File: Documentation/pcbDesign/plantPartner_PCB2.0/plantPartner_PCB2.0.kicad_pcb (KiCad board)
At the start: 2 copper layers, 70 x 65.1 mm, 76 parts, among them IC1 MPM3610, J1 Conn_01x04, J10 Screw_Terminal_01x02, J11 Conn_01x02, J12 Conn_01x03, J13 Conn_01x03, J14 Conn_01x03, J15 Conn_01x03, J16 Conn_01x01, J17 Conn_01x03, J18 Conn_01x03, J19 Conn_01x04, J2 Conn_01x04, J20 Conn_01x04, J21 Conn_01x05, J22 Conn_01x04, J23 Conn_01x01, J25 Conn_01x01, J26 Conn_01x01, J27 Conn_01x01, J28 Conn_01x01, J29 Conn_01x02, J3 Conn_01x04, J30 Screw_Terminal_01x02, J4 Screw_Terminal_01x04, J5 Conn_01x02, J6 Barrel_Jack, J7 Screw_Terminal_01x02, J8 Conn_01x01, J9 Screw_Terminal_01x02, Q1 AO3400A, Q2 AO3400A, Q4 AO3400A, U2 MAX485, U3 ESP32-DEVKIT-V1

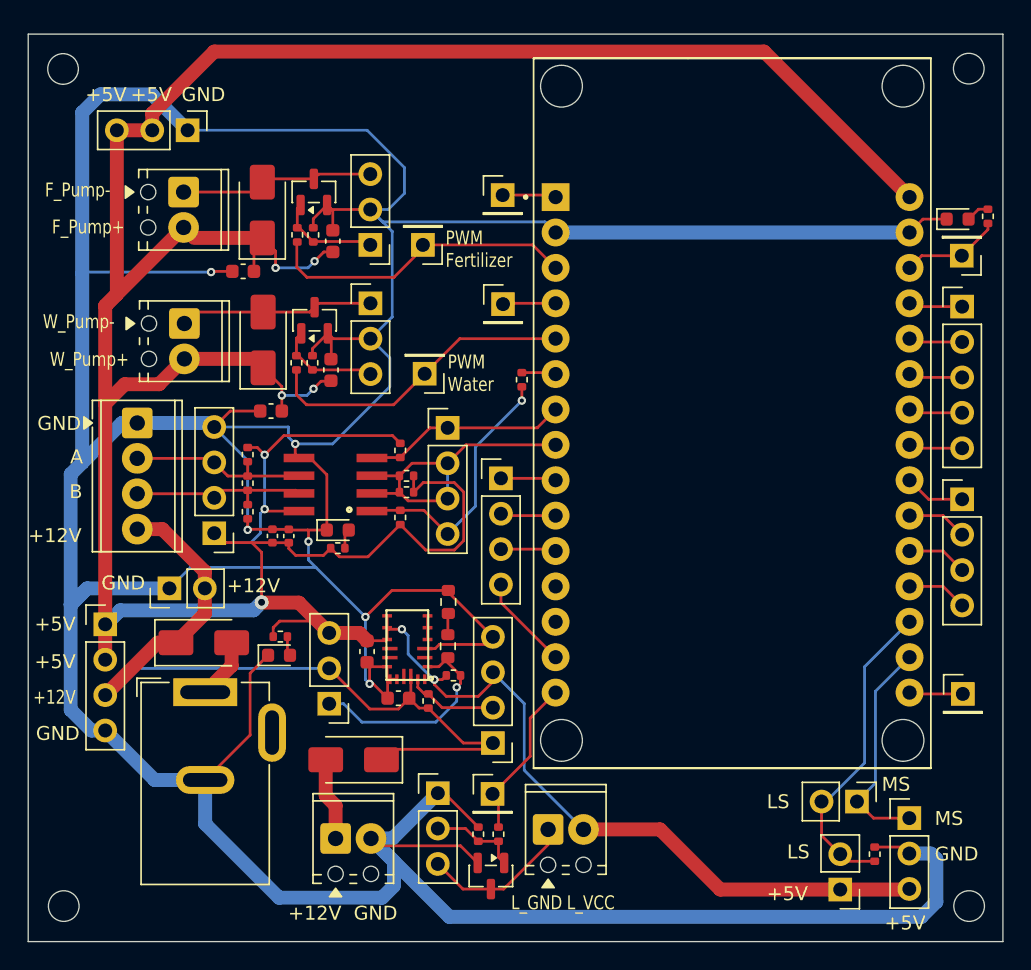
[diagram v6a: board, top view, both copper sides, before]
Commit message: I made an oopsie with PCBv2 order so I had to fix that and in the meantime I found a cheaper solution that kept the same logic of the circuits. It saved us 0 yippee
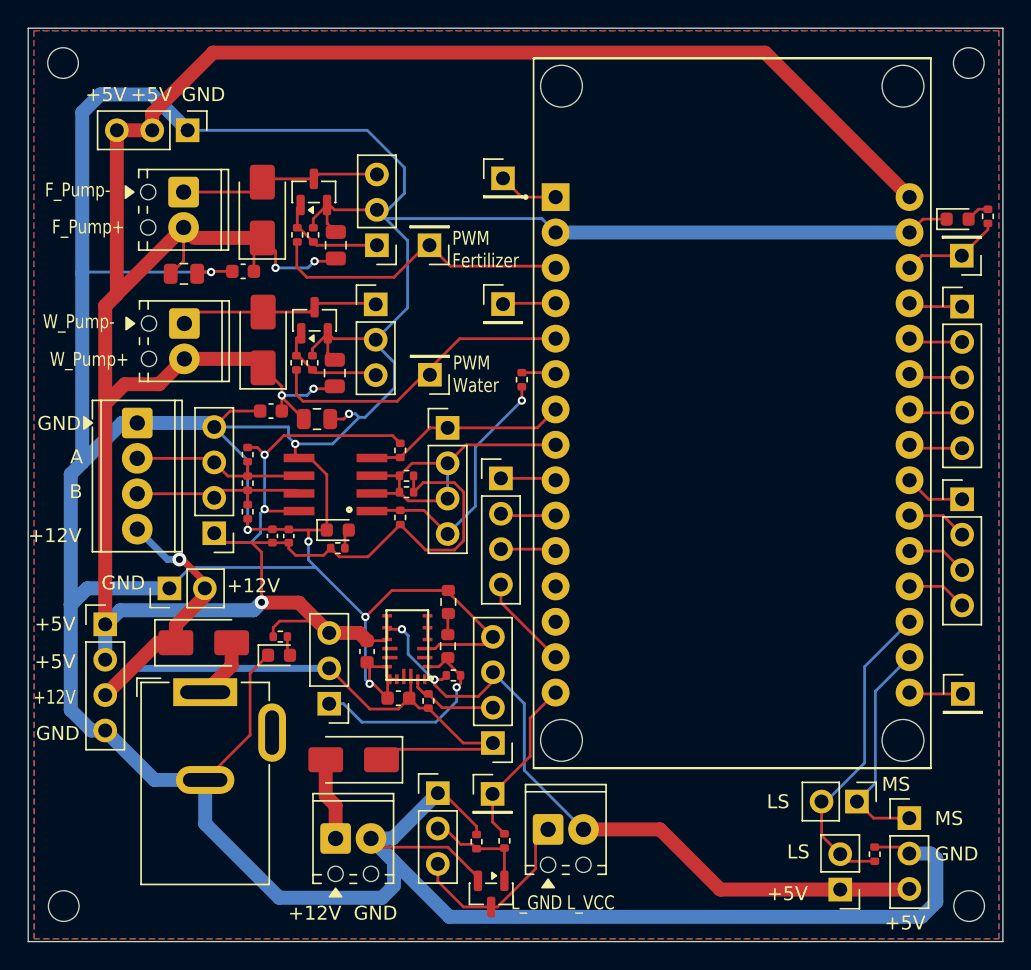
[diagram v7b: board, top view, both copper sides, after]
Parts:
- added C10: 47uF, Capacitor_SMD:C_0805_2012Metric, F.Cu at (71.5, 41.5)
- added C9: 47uF, Capacitor_SMD:C_0805_2012Metric, F.Cu at (81.0, 52.0)
- C5, C6: value 220uF -> 47uF; footprint Capacitor_SMD:C_0603_1608Metric -> Capacitor_SMD:C_0805_2012Metric
- moved Q4 1.28 mm to (93.5, 86.0)
- moved J28 1.20 mm to (94.4, 34.7)
- moved R25 0.64 mm to (94.5, 82.2)
- moved R27 0.55 mm to (92.5, 82.3)
- moved J13 0.48 mm to (85.3, 39.5)
- moved J27 0.48 mm to (89.1, 39.5)
- moved REF** 0.43 mm to (62.8, 26.4)
- moved REF** 0.40 mm to (127.8, 26.4)
- moved J12 0.38 mm to (85.3, 43.7)
- moved J26 0.38 mm to (89.2, 48.8)
- moved C5 0.36 mm to (82.4, 39.5)
- moved C6 0.36 mm to (82.3, 48.6)
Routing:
- net GND: track 381.5 -> 389.1 mm, vias 6 -> 7
- net +5V: track 286.7 -> 294.2 mm
- net /L_Drain: track 11.1 -> 13.4 mm
- net /LAMP_PIN: track 11.7 -> 13.0 mm
- net /L_Gate: track 6.45 -> 7.75 mm
- net /F_Gate: track 7.51 -> 8.37 mm
- net +12V: track 60.3 -> 59.9 mm, vias 0 -> 1
- added copper zone on B.Cu, net GND
- added copper zone on F.Cu, net GND
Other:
- board size 70 x 65.1 mm -> 70 x 65.6 mm

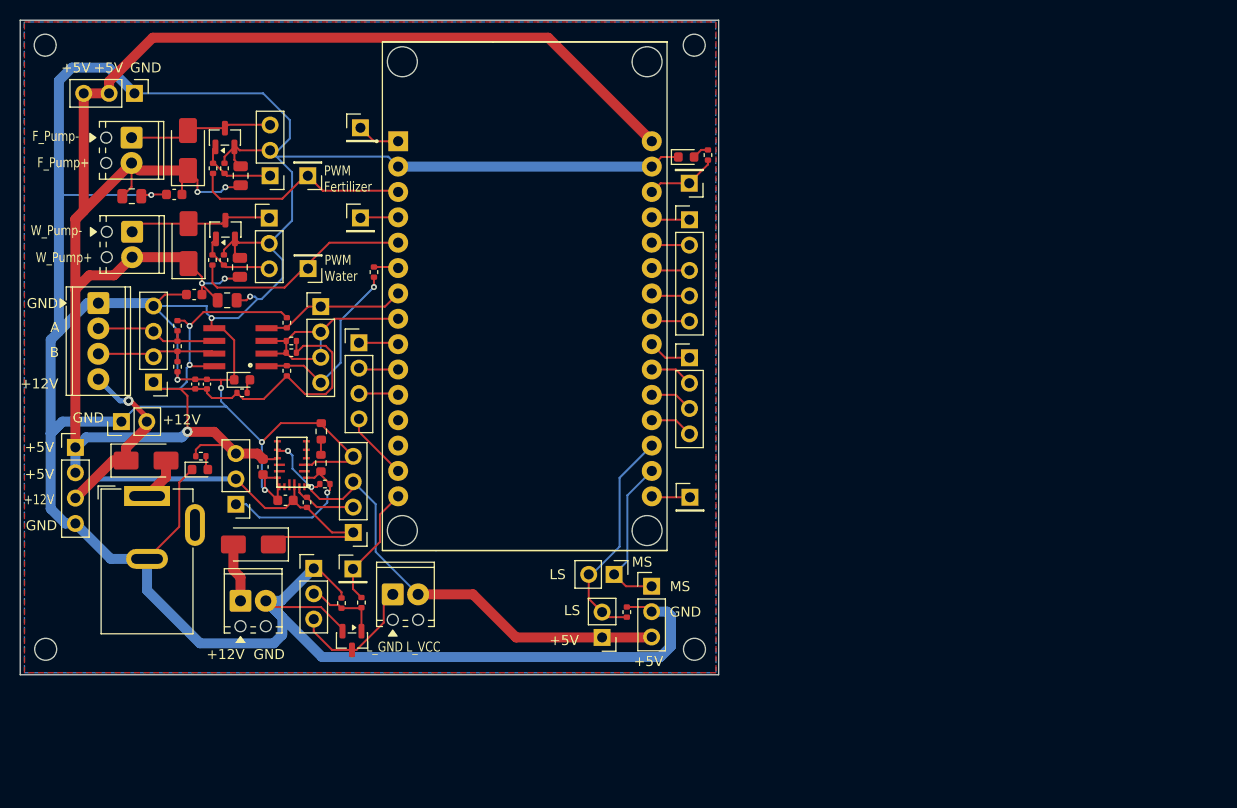
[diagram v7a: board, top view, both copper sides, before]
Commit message: Worked on RC Documentation
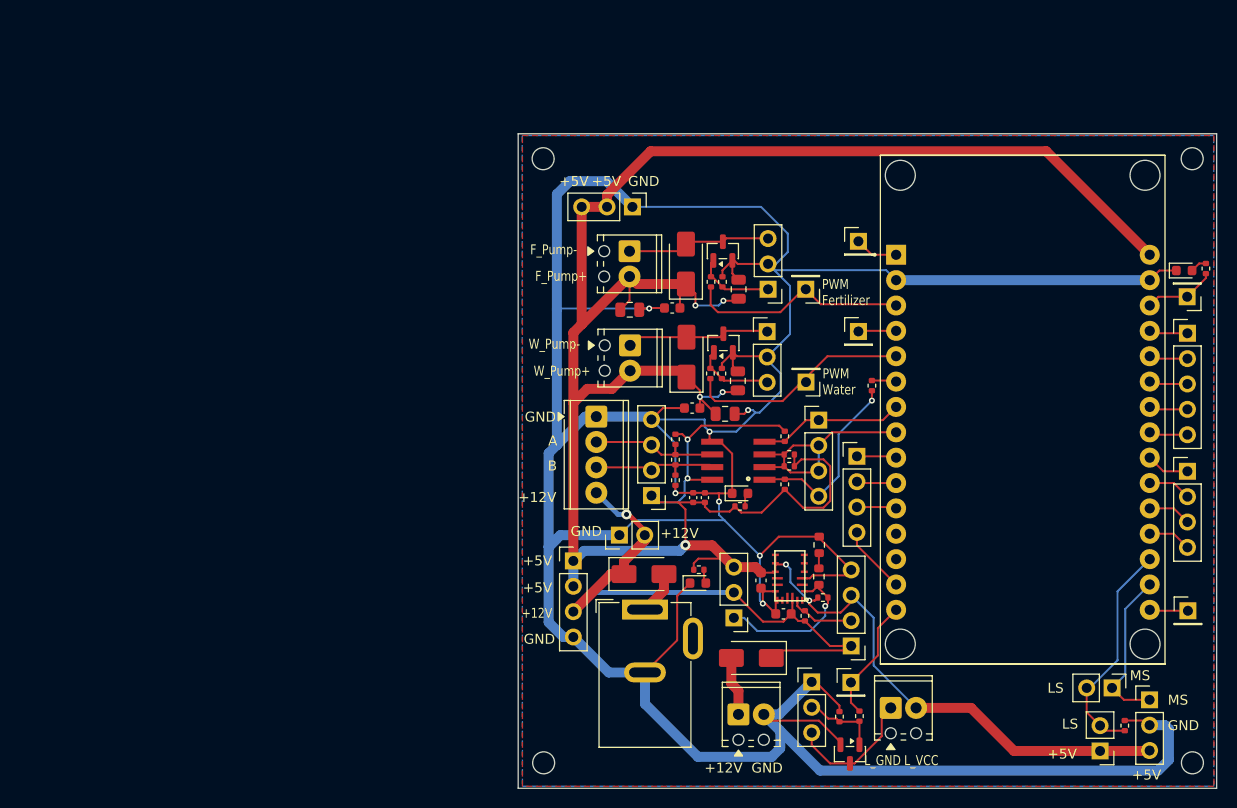
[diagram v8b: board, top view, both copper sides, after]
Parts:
- moved C10 51.1 mm to (121.4, 52.9)
- moved C3 51.1 mm to (127.7, 71.7)
- moved C5 51.1 mm to (132.3, 50.8)
- moved C7 51.1 mm to (125.6, 52.7)
- moved C8 51.1 mm to (127.6, 62.7)
- moved D10 51.1 mm to (176.9, 49.0)
- moved D2 51.1 mm to (122.8, 79.4)
- moved D5 51.1 mm to (127.0, 48.3)
- moved IC1 51.1 mm to (137.4, 79.5)
- moved J10 51.1 mm to (121.3, 47.0)
- moved J11 51.1 mm to (120.3, 75.5)
- moved J13 51.1 mm to (135.2, 50.8)
- moved J16 51.1 mm to (177.3, 83.0)
- moved J17 51.1 mm to (173.4, 92.0)
- moved J18 51.1 mm to (121.6, 42.6)
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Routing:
- net +5V: track 294.2 -> 291.6 mm
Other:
- board size 70 x 65.6 mm -> 70 x 65.5 mm
